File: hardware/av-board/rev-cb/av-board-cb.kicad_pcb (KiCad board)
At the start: 4 copper layers, 130 x 100 mm, 295 parts, among them J1 RCA Y, J11 XIAO 5V..D7, J12 XIAO D0..D6, J13 OPTICAL, J14 RCA S/PDIF, J15 USB-C 5V, J16 JTAG, J2 RCA Pb, J20 DF40HC(3.0)-80DS, J21 DF40HC(3.0)-100DS, J22 DF40HC(3.0)-100DS, J3 RCA Pr, J4 RCA L, J5 RCA R, J6 HDMI-001, J7 SYNC, J8 VGA, Q1 2N7002, Q2 2N7002, Q3 2N7002, Q4 2N7002, Q5 2N7002, SW1 TS-1187A-B-A-B, SW2 TS-1187A-B-A-B, SW3 TS-1187A-B-A-B, U1 ADV7181DBCPZ-RL, U10 TPD4E05U06DQAR, U12 TPS7A2045PDBVR, U13 SN74LVC1GU04DBVR, U14 SN74LVC1G04DBVR, U15 SN74LVC1G04DBVR, U17 MS5351M, U18 ME6211C25M5G-N, U19 TPD4E05U06DQAR, U2 SN65DP159RGZR, U20 TPD4E05U06DQAR, U21 SN74LVC2G17DBVR, U22 SN74LVC8T245PWR, U23 SN74AVC4T245PWR, U24 ME6211C30M5G-N, U3 PCM1808PWR, U4 TLV62569DBVR, U5 TPS7A7001DDAR, U6 TPS7A7001DDAR, U7 TLV62569DBVR, U8 TPD4E05U06DQAR, U9 TPD4E05U06DQAR, Y1 28.63636MHz 20pF, Y2 25MHz 10pF

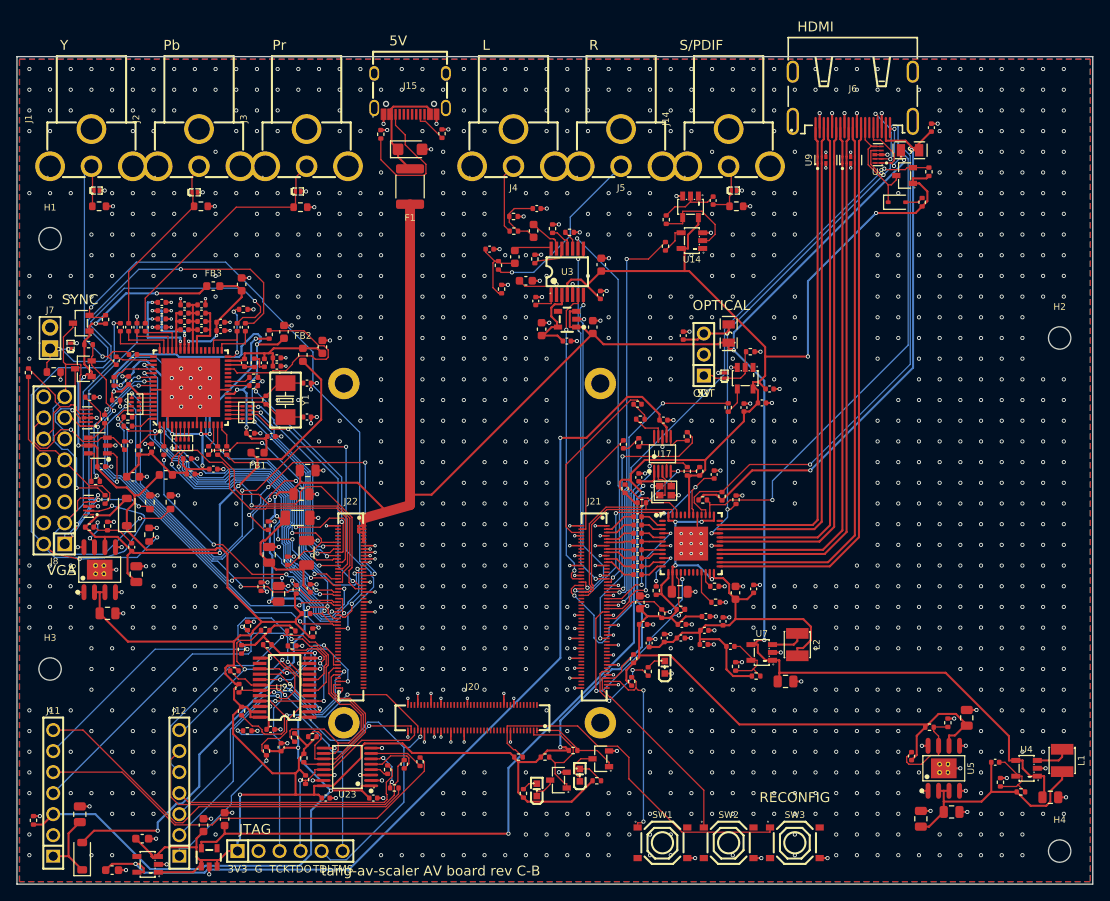
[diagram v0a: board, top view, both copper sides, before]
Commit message: AV boards: the last complete, valid design of each revision; decoupling at the pins
Each revision's board, schematic, fab files and renders are its last complete
route: DRC clean, no unconnected items, ERC clean, the board equal to its
schematic part for part (pads, values, footprints; only the mounting holes
H1-H4 have no symbol).

- Rev A: the silkscreen pass (labels clear of pads, texts and part bodies);
  copper unchanged.
- Rev B: the previous route with the silkscreen pass. Its schematic stays the
  one it was routed from: board.py now numbers eight capacitors the other way
  round, and its placement fixes (below) are not routed yet, the routes on the
  new placement having left 1 and 3 connections (review.md, Status).
- C-A: routed again on the fixed placement (try-ca-p1), the copper the router
  laid twice over taken up (218 segments).
- C-B: S/PDIF on rev B's 5-pin header instead of the coax jack, the HDMI
  receptacle next to the RCAs, the board 100 x 100 mm; routed again on the
  fixed placement (try-cb-p3). 5.4 mm of copper laid side by side in five
  nets is left (rev-c/review.md).

The review found decoupling not at the pins on every board (ADV7511 9-25 mm,
DP159 6-13 mm, the bucks' input capacitor by EN, the LDOs' capacitors, the
clock LDOs 73-80 mm from their chip) and C's VBUS_IN 0.25 mm wide for 2 A:
- parts.py: Part.at = "REF.PAD", the one pad a capacitor or filter serves;
  circuits, carrier.py and board.py name it for every regulator and supply pin
- pcbkit.py placer: ESD parts first, then small chips, then the at= capacitors
  and bias parts in board.py order; mean pin-to-capacitor distance on the
  placements: rev B 8.1 -> 3.6 mm, C-A 6.3 -> 3.3, C-B 5.5 -> 3.4
- rev C: VBUS_IN 0.7/1.2 mm into the TVS and fuse; rev B and C: the coax
  slicer placed first (SPDIF_AC a bias net); rev B: the buck U4 turned over

Kit: the silkscreen pass (labels clear of pads, texts, parts and the SOM,
reserved in the placer); prune takes up copper lying on another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
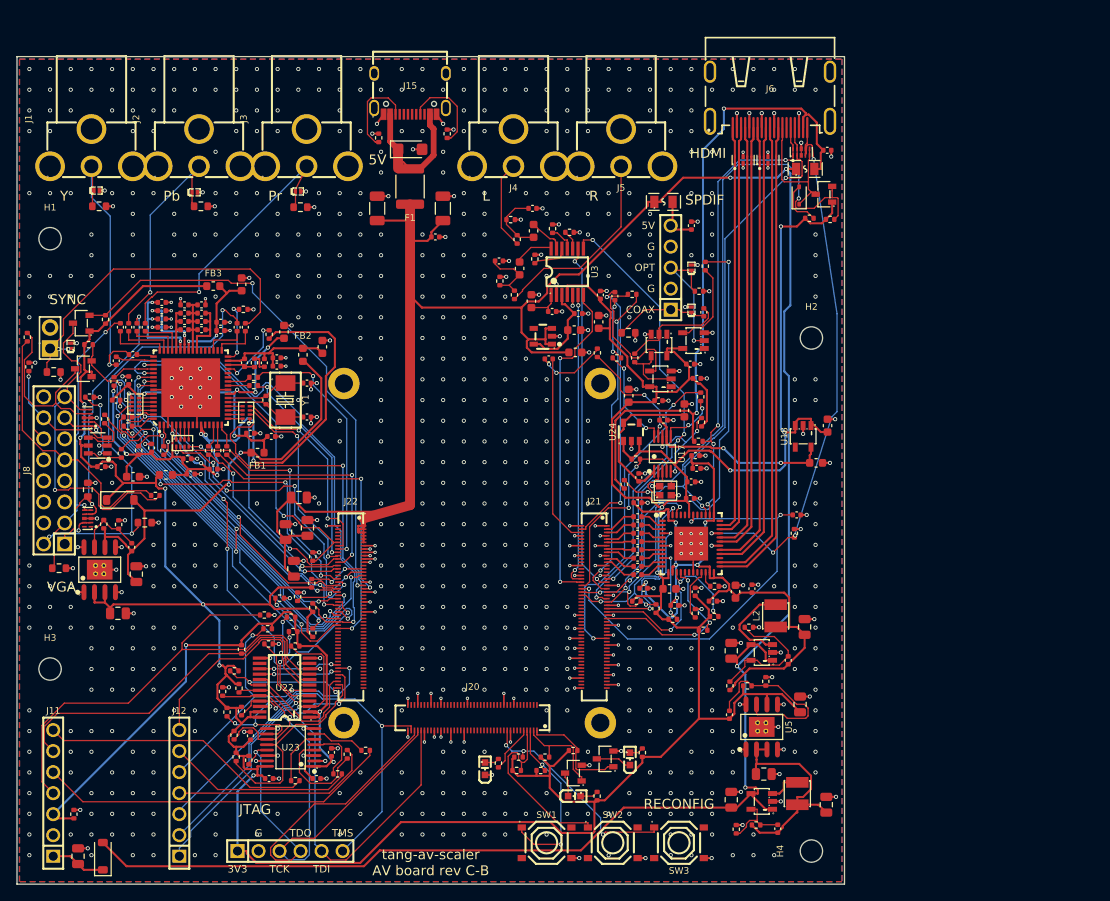
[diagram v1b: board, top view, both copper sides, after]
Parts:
- removed J14: RCA S/PDIF, lcsc:CONN-TH_RCJ-011
- C11, C8: value 10u -> 220p; footprint Capacitor_SMD:C_0805_2012Metric -> Capacitor_SMD:C_0402_1005Metric
- C12, C9: value 220p -> 10u; footprint Capacitor_SMD:C_0402_1005Metric -> Capacitor_SMD:C_0805_2012Metric
- C5, C85: value 10u -> 6.8p; footprint Capacitor_SMD:C_0805_2012Metric -> Capacitor_SMD:C_0402_1005Metric
- C6, C86: value 6.8p -> 10u; footprint Capacitor_SMD:C_0402_1005Metric -> Capacitor_SMD:C_0805_2012Metric
- J13: value OPTICAL -> SPDIF; footprint lcsc:HDR-TH_3P-P2.54-V-M_PZ254V-11-03P -> lcsc:HDR-TH_5P-P2.54-V-M
- moved C79 98.3 mm to (196.6, 99.1)
- moved C78 96.7 mm to (197.9, 94.6), turned to 90 degrees
- moved U18 94.6 mm to (195.0, 95.9), turned to 90 degrees
- moved C77 74.3 mm to (180.6, 92.8)
- moved C76 73.0 mm to (173.9, 91.0)
- moved U24 72.4 mm to (174.2, 95.3)
- moved C3 45.1 mm to (150.6, 71.8), turned to 0 degrees
- moved C1 44.8 mm to (151.5, 68.3)
- moved C2 38.6 mm to (143.5, 68.3), turned to 90 degrees
- moved C4 38.6 mm to (186.3, 139.8), turned to 90 degrees
- moved R4 32.4 mm to (186.9, 143.4)
- moved L1 32.2 mm to (194.3, 139.1)
- moved R3 32.2 mm to (189.3, 142.9)
- moved U4 32.2 mm to (190.0, 140.0)
- moved H2 30.0 mm to (196.0, 84.0)
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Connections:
- C11 pad 2: GND -> FB_1V8A
- C12 pad 2: FB_1V8A -> GND
- C5 pad 2: GND -> FB_3V6
- C6 pad 2: FB_3V6 -> GND
- C8 pad 2: GND -> FB_3V3
- C85 pad 2: GND -> FB_1V1
- C86 pad 2: FB_1V1 -> GND
- C9 pad 2: FB_3V3 -> GND
- J13 pad 1: SPDIF_OPT -> SPDIF_COAX
- J13 pad 3: SPDIF_5V -> SPDIF_OPT
- J20 pad 71: (no net) -> IN_LED
- J20 pad 73: (no net) -> IN_KEY2
- J20 pad 75: (no net) -> IN_KEY1
- J21 pad 11: IN_LED -> (no net)
- J21 pad 5: IN_KEY1 -> (no net)
- J21 pad 7: IN_KEY2 -> (no net)
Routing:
- net 2V5: track 113.5 -> 23.4 mm
- net 3V0: track 91.8 -> 18.5 mm, vias 2 -> 0
- net VGA_VSIN: track 7.82 -> 50.4 mm, vias 2 -> 4
- net VGA_G: track 103.2 -> 61.2 mm
- net 3V3: track 492.1 -> 452.1 mm, vias 10 -> 11
- net AV_DVDDIO: track 57.6 -> 89.5 mm, vias 6 -> 8
- net IN_Y7: track 72.3 -> 42.3 mm, vias 4 -> 2
- net MODE1: track 36.4 -> 9.45 mm, vias 4 -> 2
- net JTAG_TDO: track 25.9 -> 46.3 mm
- net SER_REFCLK_P: track 13.2 -> 33.2 mm, vias 0 -> 2
- net SPDIF_ORX: track 34.8 -> 54.5 mm
- net DP_OE: track 30.8 -> 50.2 mm, vias 4 -> 3
- net MODE2: track 35.7 -> 16.9 mm, vias 4 -> 2
- net VGA_R: track 56.9 -> 38.3 mm, vias 6 -> 2
- net 1V1: track 69.3 -> 86.7 mm, vias 4 -> 6
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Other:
- board size 130 x 100 mm -> 100 x 100 mm
- board text added: "COAX"
- board text added: "OPT"
- board text added: "SPDIF"
- board text removed: "OPTICAL"
- board text removed: "OUT"
- board text removed: "S/PDIF"

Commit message: AV boards: rev B, C-B routed on the fixed placement; prune side-by-side copies; JLC jack rotation
Every revision: schematic = board.py, the board = its schematic part for part,
ERC and DRC clean, no unconnected items; rev B's, C-A's and C-B's review tables
measured on these routes.

- Rev B: routed on the capacitor placement fixes (try-b-r1, its last gap
  finished); schematic regenerated (eight capacitors renumbered).
- C-B: the 1V1 buck's inductor and output capacitor placed before its feedback
  divider: in the 3V6 bucks' order the divider's 6.8 pF took the inductor's place
  beside SW, the inductor went above the chip with its SW pad turned away (10.7 mm
  of SW track, FB's copper 0.2 mm from it). Routed again (try-cb-q3): SW 4.1 mm,
  FB 3.0 mm from it; nothing digital within 0.5 mm of an analog line but XTAL1
  beside LLC at the pins' pitch.
- C-A: its review column measured on the route; CPL jack rotations.
- kit/pcbkit.py prune: copper laid side by side taken up too (beside(): the
  shorter of each kit/doubled.py pair), every candidate checked by DRC on a copy
  of the file's text first (save_without(), removable()), so nothing taken out of
  a pcbnew board is put back; rounds run with faulthandler and report a crash's
  signal (one round had segfaulted in libstdc++ with no message).
- kit/pcbkit.py finish_unconnected: a gap's three nearest pad pairs tried in turn
  (rev B's TX_PLVDD pin 21 was walled in towards pin 26, not towards its own
  capacitor).
- kit/gen_fab.py JLC_TURN: JLCPCB places a part by its own footprint for the LCSC
  number; for RCJ-014 and RCJ-017 that is ours turned 90 degrees, so the CPL
  turns those jacks back (their preview had the barrels along the board edge).
  RCJ-012 has no footprint there and is placed as drawn.

Co-Authored-By: Claude Opus 5.5 <noreply@anthropic.com>
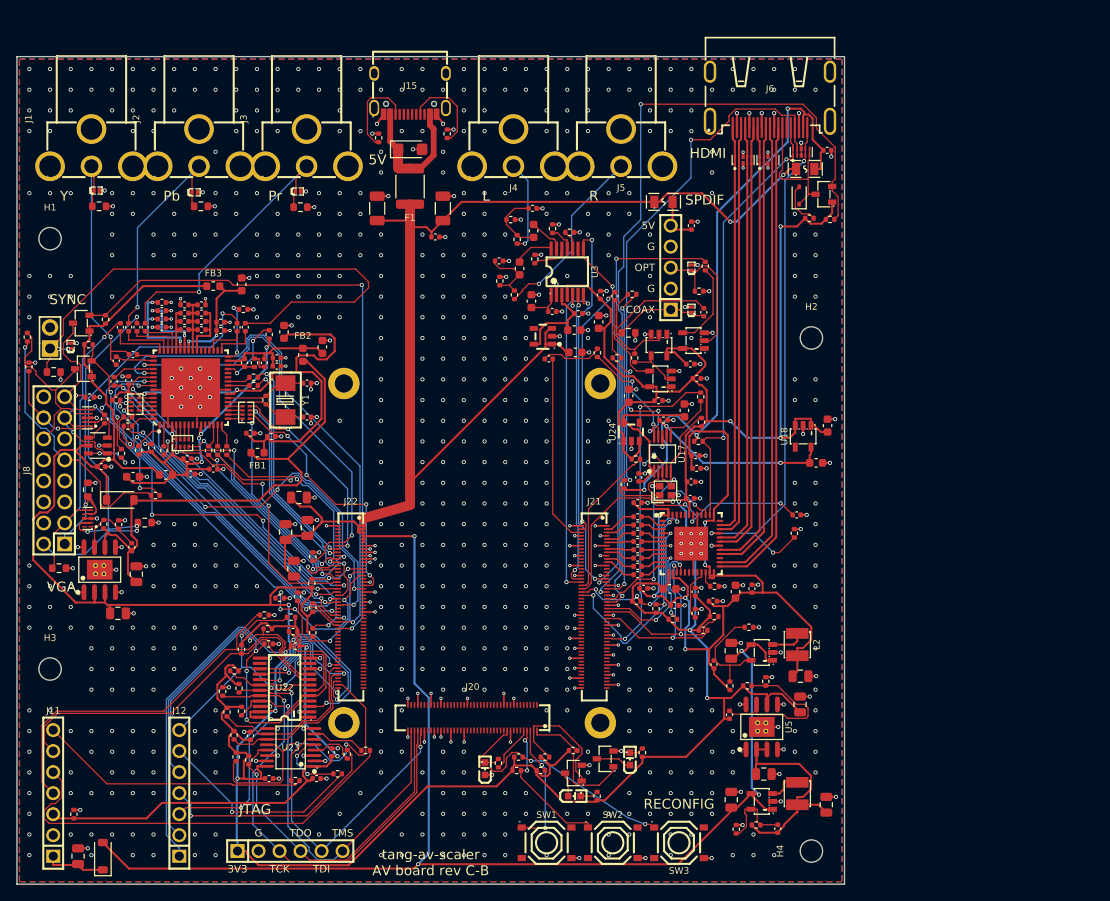
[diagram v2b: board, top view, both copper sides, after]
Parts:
- C85: value 6.8p -> 10u; footprint Capacitor_SMD:C_0402_1005Metric -> Capacitor_SMD:C_0805_2012Metric
- C86: value 10u -> 6.8p; footprint Capacitor_SMD:C_0805_2012Metric -> Capacitor_SMD:C_0402_1005Metric
- moved C86 11.9 mm to (184.2, 123.5)
- moved L2 4.35 mm to (194.3, 121.0)
- moved C85 2.42 mm to (194.7, 124.9), turned to 0 degrees
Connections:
- C85 pad 2: FB_1V1 -> GND
- C86 pad 2: GND -> FB_1V1
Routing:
- net VGA_VSIN: track 50.4 -> 9.42 mm, vias 4 -> 2
- net AV_DVDDIO: track 89.5 -> 58.3 mm, vias 8 -> 6
- net RCA_SYNC: track 42.8 -> 67.1 mm
- net 1V1: track 86.7 -> 108.9 mm
- net AV_DVDD: track 41.3 -> 63.3 mm, vias 5 -> 2
- net XIAO_D0: track 37.9 -> 57.9 mm, vias 1 -> 3
- net XIAO_D1: track 32.7 -> 51.7 mm, vias 1 -> 3
- net IN_Y4: track 55.0 -> 37.1 mm, vias 4 -> 2
- net CEC_FPGA: track 82.9 -> 99.4 mm
- net HDMI_SDA: track 63.5 -> 79.9 mm, vias 3 -> 4
- net +5V: track 331.3 -> 315.8 mm, vias 4 -> 6
- net IN_Y6: track 54.1 -> 40.7 mm
- net ESP_IRQ: track 25.5 -> 37.6 mm, vias 0 -> 2
- net DP_OE: track 50.2 -> 38.2 mm
- net 3V3: track 452.1 -> 464.0 mm, vias 11 -> 9
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
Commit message: AV boards: silkscreen to JLCPCB's limits; the XIAO's way in printed on rev C
JLCPCB's silkscreen limits (its capabilities page): lines and strokes 0.15 mm
at least, text 1 mm high with a 1:6 stroke, 0.15 mm from pads.

- kit/pcbkit.py: designators and pin labels 1 mm (were 0.8 and 0.9 mm), every
  text's stroke 1:6 of its height; designators clear of the other parts'
  bodies, tried at 40 places beside their part before its own body.
  silk_tidy(): the parts' own silkscreen widened to 0.15 mm and cut back where
  it came within 0.15 mm of a pad, past the board's edge, under a text or onto
  another part's (the bigger parts first); EasyEDA's 0.12 mm pin 1 dots (too
  small to print) taken out, small marks moved clear. A second run changes
  nothing.
- Rev B, C-A, C-B: the silkscreen pass run again (--silk): only the silkscreen
  Gerbers changed. DRC: no silkscreen warnings (were 56, 63, 54); designators
  shown 36, 51, 45 (were 35, 41, 33). The trimmed footprints now differ from
  the library (DRC's lib_footprint_mismatch, noted in the reviews).
- Rev B: "XIAO, USB >" by J12 (by J11 no place was clear: it lay over copper).
- Rev C: the XIAO's way in printed beside J12, "XIAO, USB >" reading down to
  its USB-C's end (that of D0 and 5V, the sockets' pin 1, at the bottom edge);
  kit SILK_NEAR entries may carry an angle (the label beside the part).

Co-Authored-By: Claude Opus 5.5 <noreply@anthropic.com>
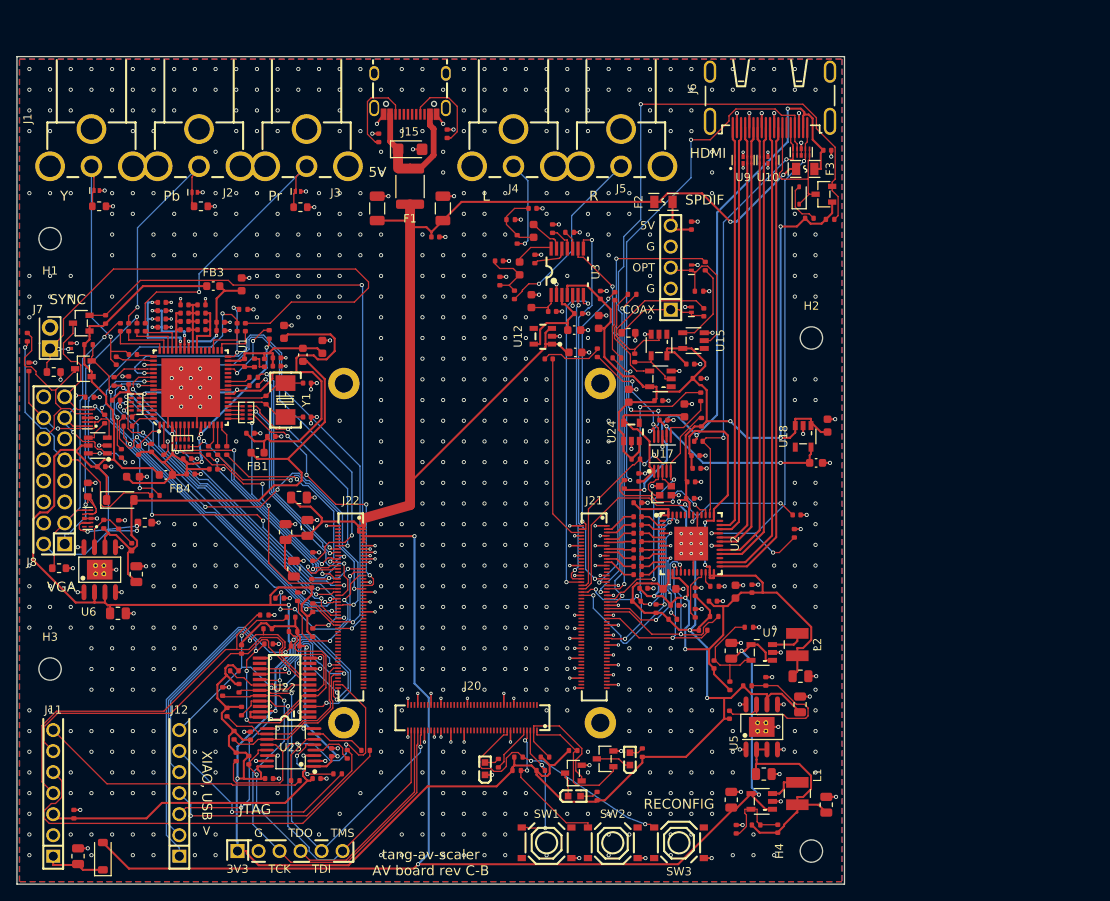
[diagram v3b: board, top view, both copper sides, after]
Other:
- board text added: "XIAO, USB >"
